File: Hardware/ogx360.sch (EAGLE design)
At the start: 29 parts, among them J1 USB_A_SMT_FEMALE_NS, SW1 TL3305AF160QG, U1 MAX3421ETQFP32-5MM, U2 74HC4050, U3 MIC5219-3.3YM5-TR, U4 ARDUINO_LEONARDO_MICRO, U5 ARDUINO_LEONARDO_MICRO, U6 ARDUINO_LEONARDO_MICRO, U7 ARDUINO_LEONARDO_MICRO, Y1 12MHz

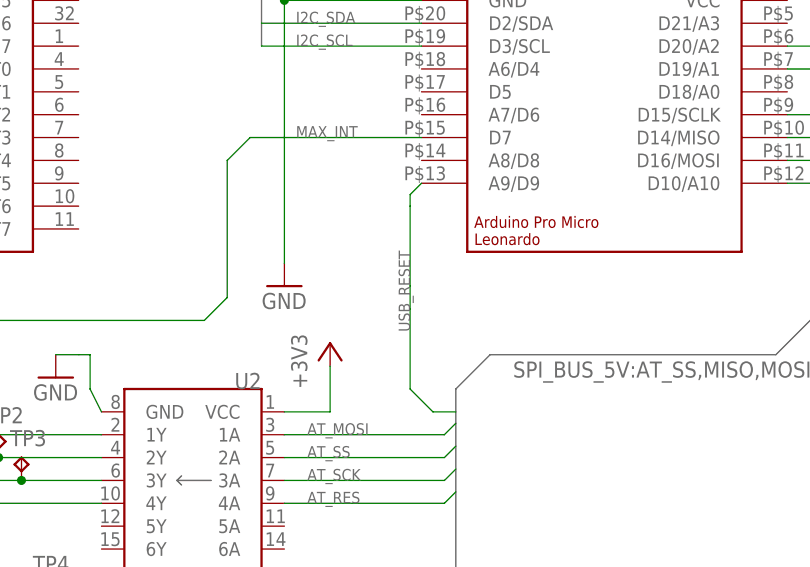
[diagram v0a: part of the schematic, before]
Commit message: HW: Route reset trace
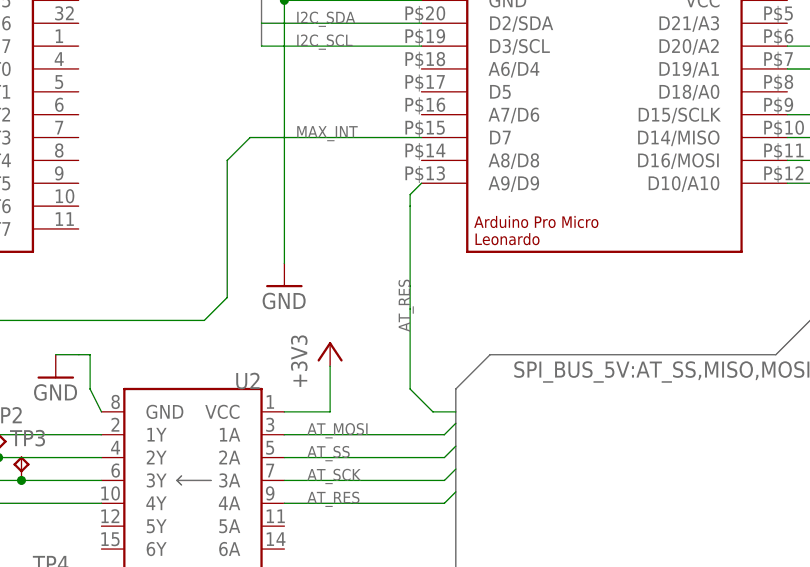
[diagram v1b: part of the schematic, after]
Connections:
- removed net USB_RESET: U4.A9/D9
- net AT_RES: now also U4.A9/D9
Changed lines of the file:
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@@
 <setting verticaltext="up"/>
 </settings>
-<grid distance="0.1" unitdist="inch" unit="inch" style="lines" multiple="1" display="yes" altdistance="0.05" altunitdist="inch" altunit="inch"/>
+<grid distance="0.1" unitdist="inch" unit="inch" style="lines" multiple="1" display="no" altdistance="0.01" altunitdist="inch" altunit="inch"/>
 <layers>
 <layer number="1" name="Top" color="4" fill="1" visible="no" active="no"/>
@@
 </segment>
 </net>
-<net name="USB_RESET" class="0">
-<segment>
-<wire x1="160.02" y1="106.68" x2="157.48" y2="106.68" width="0.1524" layer="91"/>
-<wire x1="157.48" y1="106.68" x2="154.94" y2="109.22" width="0.1524" layer="91"/>
-<wire x1="154.94" y1="118.11" x2="154.94" y2="120.65" width="0.1524" layer="91"/>
-<wire x1="154.94" y1="129.54" x2="154.94" y2="120.65" width="0.1524" layer="91"/>
-<label x="154.94" y="115.57" size="1.27" layer="95" rot="R90"/>
-<pinref part="U4" gate="G$1" pin="A9/D9"/>
-<wire x1="156.21" y1="132.08" x2="154.94" y2="130.81" width="0.1524" layer="91"/>
-<wire x1="154.94" y1="130.81" x2="154.94" y2="129.54" width="0.1524" layer="91"/>
-<wire x1="154.94" y1="109.22" x2="154.94" y2="118.11" width="0.1524" layer="91"/>
-</segment>
-</net>
 <net name="VBCOMP" class="0">
 <segment>
@@
 <pinref part="U2" gate="G$1" pin="4A"/>
 </segment>
+<segment>
+<wire x1="160.02" y1="106.68" x2="157.48" y2="106.68" width="0.1524" layer="91"/>
+<wire x1="157.48" y1="106.68" x2="154.94" y2="109.22" width="0.1524" layer="91"/>
+<wire x1="154.94" y1="118.11" x2="154.94" y2="120.65" width="0.1524" layer="91"/>
+<wire x1="154.94" y1="129.54" x2="154.94" y2="120.65" width="0.1524" layer="91"/>
+<label x="154.94" y="115.57" size="1.27" layer="95" rot="R90"/>
+<pinref part="U4" gate="G$1" pin="A9/D9"/>
+<wire x1="156.21" y1="132.08" x2="154.94" y2="130.81" width="0.1524" layer="91"/>
+<wire x1="154.94" y1="130.81" x2="154.94" y2="129.54" width="0.1524" layer="91"/>
+<wire x1="154.94" y1="109.22" x2="154.94" y2="118.11" width="0.1524" layer="91"/>
+</segment>
 </net>
